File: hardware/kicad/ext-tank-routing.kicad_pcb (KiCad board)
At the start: 2 copper layers, 120 x 80 mm, 16 parts, among them K201 G6K-2F-Y-DC5, K202 G6K-2F-Y-DC5, K203 G6K-2F-Y-DC5, K204 G6K-2F-Y-DC5, P201 JIO-WETSEND, P202 JTR-PRI, P203 JTR-SEC, P204 JTR-XFADE, P205 JFB-INJ, P206 JER-CTRL, P207 JER-PWR, U201 OPA1679IDR

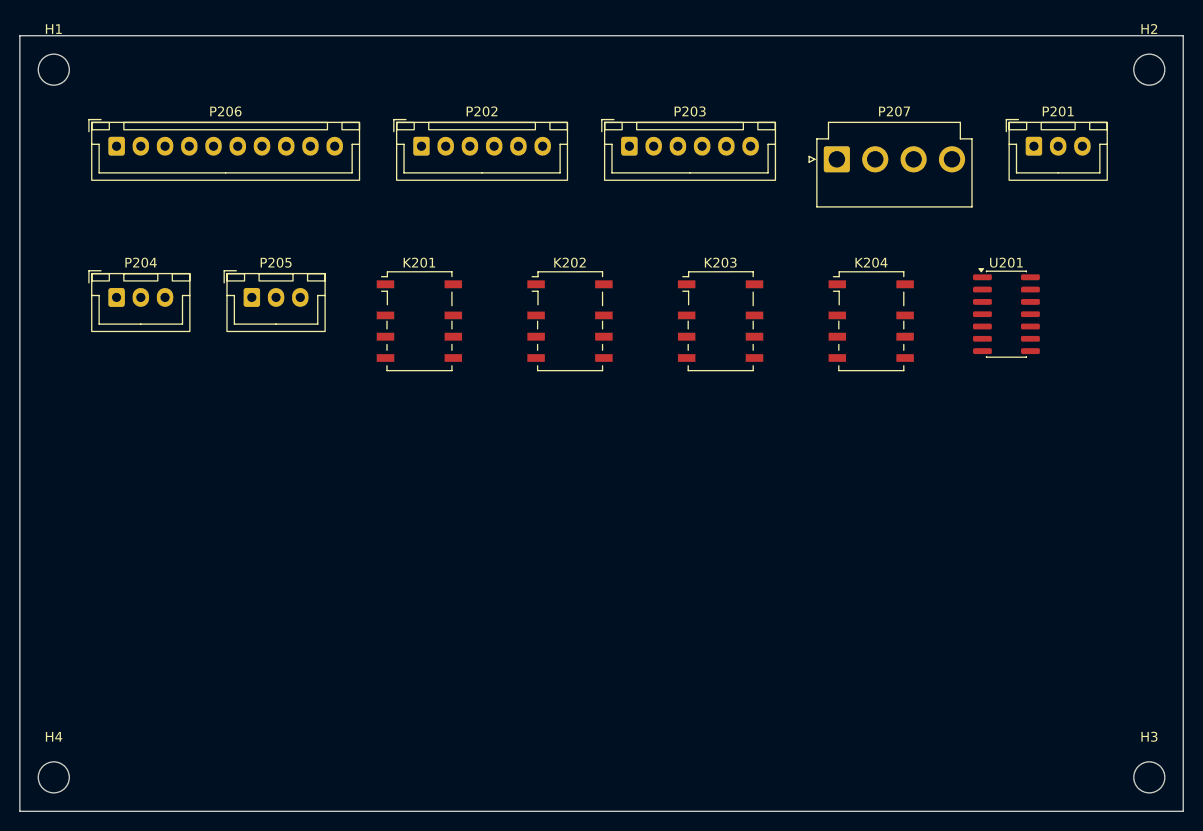
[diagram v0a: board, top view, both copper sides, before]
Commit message: Rev A: 3-pass schematic review + fixes, PCB sync + placement, parts freeze (2026-07-31)
Pass1+2 fixed cross-channel shorts (io rails/C1-C4/alias columns), ext-tank ghost wiring, U201 unit un-stack, U101-104 power units, PS500 pinout from datasheet, DRV renames. Decisions: TQ2-5V relays +D301, R241-3 deleted, PGND_IN+R502 link, K401-403 clip decoder, RCJ-041 tank jacks. GAS_Parts lib (TQ2/URA_YMD/RCJ-041), ~203 footprints, 6 boards synced+placed DRC-clean. Pass3 visual: paper sizes, stale notes. 3D GLBs + viewer. See hardware/kicad/schematic_review.md
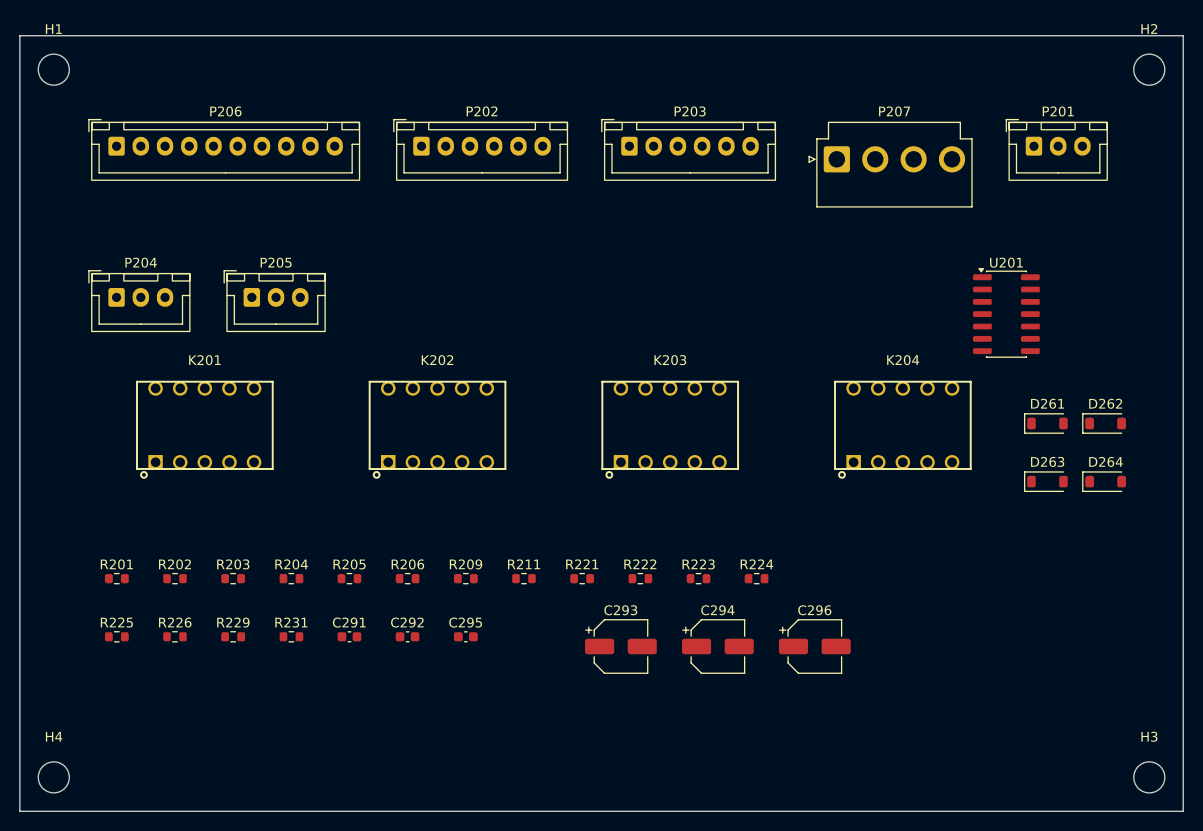
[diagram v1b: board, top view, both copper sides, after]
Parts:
- added C291: 100nF, Capacitor_SMD:C_0603_1608Metric, F.Cu at (34.0, 62.0)
- added C292: 100nF, Capacitor_SMD:C_0603_1608Metric, F.Cu at (40.0, 62.0)
- added C293: 10uF, Capacitor_SMD:CP_Elec_5x5.8, F.Cu at (62.0, 63.0)
- added C294: 10uF, Capacitor_SMD:CP_Elec_5x5.8, F.Cu at (72.0, 63.0)
- added C295: 100nF, Capacitor_SMD:C_0603_1608Metric, F.Cu at (46.0, 62.0)
- added C296: 10uF, Capacitor_SMD:CP_Elec_5x5.8, F.Cu at (82.0, 63.0)
- added D261: 1N4148W, Diode_SMD:D_SOD-123, F.Cu at (106.0, 40.0)
- added D262: 1N4148W, Diode_SMD:D_SOD-123, F.Cu at (112.0, 40.0)
- added D263: 1N4148W, Diode_SMD:D_SOD-123, F.Cu at (106.0, 46.0)
- added D264: 1N4148W, Diode_SMD:D_SOD-123, F.Cu at (112.0, 46.0)
- added R201: 100R, Resistor_SMD:R_0603_1608Metric, F.Cu at (10.0, 56.0)
- added R202: 20k, Resistor_SMD:R_0603_1608Metric, F.Cu at (16.0, 56.0)
- added R203: 20k, Resistor_SMD:R_0603_1608Metric, F.Cu at (22.0, 56.0)
- added R204: 20k, Resistor_SMD:R_0603_1608Metric, F.Cu at (28.0, 56.0)
- added R205: 100R, Resistor_SMD:R_0603_1608Metric, F.Cu at (34.0, 56.0)
- added R206: 100R, Resistor_SMD:R_0603_1608Metric, F.Cu at (40.0, 56.0)
- added R209: 20k, Resistor_SMD:R_0603_1608Metric, F.Cu at (46.0, 56.0)
- added R211: 100k, Resistor_SMD:R_0603_1608Metric, F.Cu at (52.0, 56.0)
- added R221: 100R, Resistor_SMD:R_0603_1608Metric, F.Cu at (58.0, 56.0)
- added R222: 20k, Resistor_SMD:R_0603_1608Metric, F.Cu at (64.0, 56.0)
- added R223: 20k, Resistor_SMD:R_0603_1608Metric, F.Cu at (70.0, 56.0)
- added R224: 20k, Resistor_SMD:R_0603_1608Metric, F.Cu at (76.0, 56.0)
- added R225: 100R, Resistor_SMD:R_0603_1608Metric, F.Cu at (10.0, 62.0)
- added R226: 100R, Resistor_SMD:R_0603_1608Metric, F.Cu at (16.0, 62.0)
- added R229: 20k, Resistor_SMD:R_0603_1608Metric, F.Cu at (22.0, 62.0)
- added R231: 100k, Resistor_SMD:R_0603_1608Metric, F.Cu at (28.0, 62.0)
- K201, K202, K203, K204: value G6K-2F-Y-DC5 -> TQ2-5V; footprint Relay_DPDT_Omron_G6K-2F-Y -> GAS_Parts:Relay_DPDT_Panasonic_TQ2
- moved K201 30.9 mm to (14.0, 44.0)
- moved K202 23.7 mm to (38.0, 44.0)
- moved K203 17.8 mm to (62.0, 44.0)
- moved K204 14.7 mm to (86.0, 44.0)
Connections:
- P201 pad 1: (no net) -> WET_SEND_L
- P201 pad 2: (no net) -> AGND
- P201 pad 3: (no net) -> WET_SEND_R
- P202 pad 1: (no net) -> PRI_SEND_L
- P202 pad 2: (no net) -> PRI_RET_L
- P202 pad 3: (no net) -> AGND
- P202 pad 4: (no net) -> PRI_SEND_R
- P202 pad 5: (no net) -> PRI_RET_R
- P202 pad 6: (no net) -> AGND
- P203 pad 1: (no net) -> SEC_SEND_L
- P203 pad 2: (no net) -> SEC_RET_L
- P203 pad 3: (no net) -> AGND
- P203 pad 4: (no net) -> SEC_SEND_R
- P203 pad 5: (no net) -> SEC_RET_R
- P203 pad 6: (no net) -> AGND
- P204 pad 1: (no net) -> TANK_MIX_L
- P204 pad 2: (no net) -> AGND
- P204 pad 3: (no net) -> TANK_MIX_R
- P205 pad 1: (no net) -> FB_RET_L
- P205 pad 2: (no net) -> AGND
- P205 pad 3: (no net) -> FB_RET_R
- P206 pad 1: (no net) -> EXTMIX_L_HI
- P206 pad 10: (no net) -> CTL_EXT_MODE_B
- P206 pad 2: (no net) -> EXTMIX_L_WIPER
- P206 pad 3: (no net) -> AGND
- P206 pad 4: (no net) -> EXTMIX_R_HI
- P206 pad 5: (no net) -> EXTMIX_R_WIPER
- P206 pad 6: (no net) -> AGND
- P206 pad 7: (no net) -> +5VAUX
- P206 pad 8: (no net) -> AGND
- P206 pad 9: (no net) -> CTL_EXT_MODE_A
- P207 pad 1: (no net) -> +15VA
- P207 pad 2: (no net) -> AGND
- P207 pad 3: (no net) -> -15VA
- P207 pad 4: (no net) -> +5VAUX
- U201 pad 1: (no net) -> U201A_OUT
- U201 pad 10: (no net) -> SEC_DRV_L
- U201 pad 11: (no net) -> -15VA
- U201 pad 12: (no net) -> SEC_DRV_R
- U201 pad 13: (no net) -> U201D_OUT
- U201 pad 14: (no net) -> U201D_OUT
- U201 pad 2: (no net) -> U201A_M
- U201 pad 3: (no net) -> AGND
- U201 pad 4: (no net) -> +15VA
- U201 pad 5: (no net) -> AGND
- U201 pad 6: (no net) -> U201B_M
- U201 pad 7: (no net) -> U201B_OUT
- U201 pad 8: (no net) -> U201C_OUT
- U201 pad 9: (no net) -> U201C_OUT
